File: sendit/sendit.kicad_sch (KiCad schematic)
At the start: 7 parts

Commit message: more work towards rev c board.
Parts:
- added H3, H4: MountingHole, MountingHole:MountingHole_2.7mm_M2.5_ISO14580, symbol Mechanical:MountingHole
- added R1, R2: 2.2k, Resistor_SMD:R_0603_1608Metric, symbol Device:R_Small_US
- H1, H2: footprint MountingHole:MountingHole_3.2mm_M3_ISO14580_Pad -> yarrboard:SMTSO30XXX; LCSC (none) -> C2916369; now in the parts list
- H5: renamed from H3; footprint MountingHole:MountingHole_3.2mm_M3_ISO14580_Pad -> yarrboard:SMTSO30XXX; LCSC (none) -> C2916369; now in the parts list
- H6: renamed from H4; footprint MountingHole:MountingHole_3.2mm_M3_ISO14580_Pad -> yarrboard:SMTSO30XXX; LCSC (none) -> C2916369; now in the parts list
- TP1, TP2: footprint TestPoint:TestPoint_THTPad_D2.0mm_Drill1.0mm -> TestPoint:TestPoint_THTPad_D1.5mm_Drill0.7mm
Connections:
- net +3.3V: now also R1.2, R2.2
- net SCL: now also R2.1
- net SDA: now also R1.1
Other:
- moved on the sheet: TP1, TP2

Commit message: power system work and layout
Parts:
- added H5: MountingHole, MountingHole:MountingHole_2.7mm_M2.5_ISO14580, symbol Mechanical:MountingHole
- added J1: Conn_01x04_MountingPin, yarrboard:JST_SH_BM04B-SRSS-TB_1x04-1MP_P1.00mm_Vertical, symbol Connector_Generic_MountingPin:Conn_01x04_MountingPin
- renumbered H5 to H6, H6 to H7
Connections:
- net +3.3V: now also J1.2 (Pin_2)
- net GND: now also J1.1 (Pin_1), J1.MP (MountPin)
- net SCL: now also J1.4 (Pin_4)
- net SDA: now also J1.3 (Pin_3)
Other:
- note added: "I2C / QWIIC"

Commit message: big change removing the usb hub and serial chip.
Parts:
- removed H4: MountingHole, MountingHole:MountingHole_2.7mm_M2.5_ISO14580, symbol Mechanical:MountingHole
- added J2: Conn_02x09_Odd_Even, Connector_PinHeader_2.54mm:PinHeader_2x09_P2.54mm_Vertical, symbol Connector_Generic:Conn_02x09_Odd_Even
- renumbered H5 to H4, H6 to H5, H7 to H6
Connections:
- net +3.3V: now also J2.2 (Pin_2)
- net GND: now also J2.1 (Pin_1)
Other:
- moved on the sheet: H4

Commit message: big routing push
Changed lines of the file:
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@@
 	(wire
 		(pts
-			(xy 153.67 87.63) (xy 157.48 87.63)
+			(xy 153.67 90.17) (xy 157.48 90.17)
 		)
 		(stroke
@@
 	(wire
 		(pts
-			(xy 146.05 77.47) (xy 157.48 77.47)
+			(xy 151.13 118.11) (xy 162.56 118.11)
 		)
 		(stroke
@@
 	(wire
 		(pts
-			(xy 153.67 90.17) (xy 157.48 90.17)
+			(xy 153.67 77.47) (xy 157.48 77.47)
 		)
 		(stroke
@@
 	(global_label "ADC_ALERT{slash}RDY2"
 		(shape input)
-		(at 153.67 90.17 180)
+		(at 153.67 77.47 180)
 		(fields_autoplaced yes)
 		(effects
@@
 		)
 		(property "Intersheetrefs" "${INTERSHEET_REFS}"
-			(at 134.4167 90.17 0)
+			(at 134.4167 77.47 0)
 			(effects
 				(font
@@
 	(global_label "ADC_ALERT{slash}RDY1"
 		(shape input)
-		(at 153.67 87.63 180)
+		(at 153.67 90.17 180)
 		(fields_autoplaced yes)
 		(effects
@@
 		)
 		(property "Intersheetrefs" "${INTERSHEET_REFS}"
-			(at 134.4167 87.63 0)
+			(at 134.4167 90.17 0)
 			(effects
 				(font
@@
 	)
 	(sheet
-		(at 133.35 74.93)
+		(at 138.43 115.57)
 		(size 12.7 3.81)
 		(exclude_from_sim no)
@@
 		)
 		(property "Sheetname" "Piezo"
-			(at 133.35 74.2184 0)
+			(at 138.43 114.8584 0)
 			(effects
 				(font
@@
 		)
 		(property "Sheetfile" "piezo.kicad_sch"
-			(at 133.35 79.3246 0)
+			(at 138.43 119.9646 0)
 			(effects
 				(font
@@
 		)
 		(pin "PIEZO" input
-			(at 146.05 77.47 0)
+			(at 151.13 118.11 0)
 			(effects
 				(font

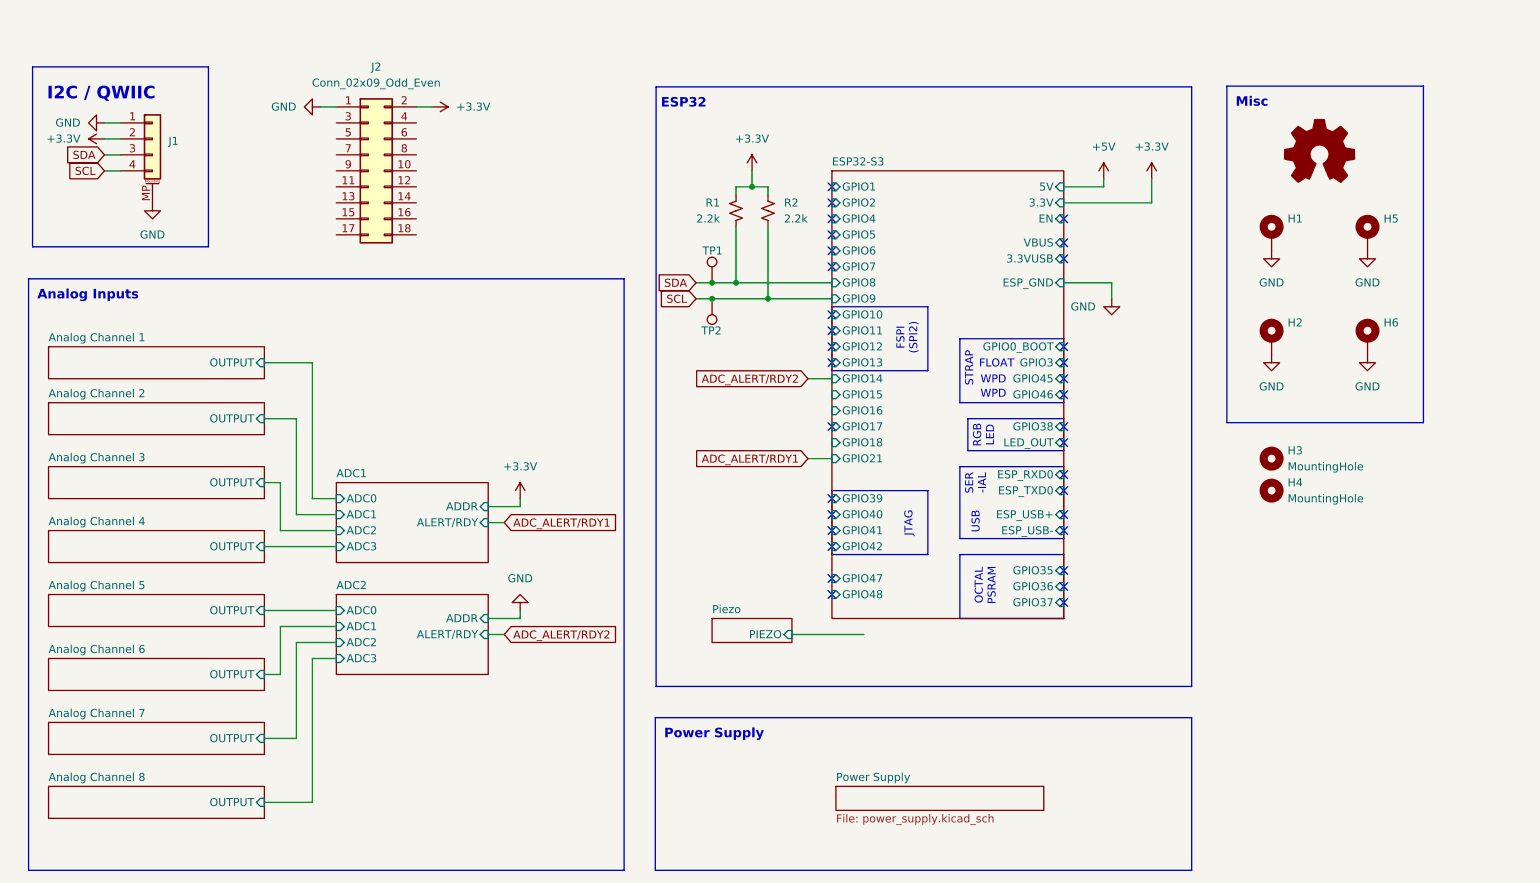
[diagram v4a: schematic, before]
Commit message: finished extra pin selection + routing
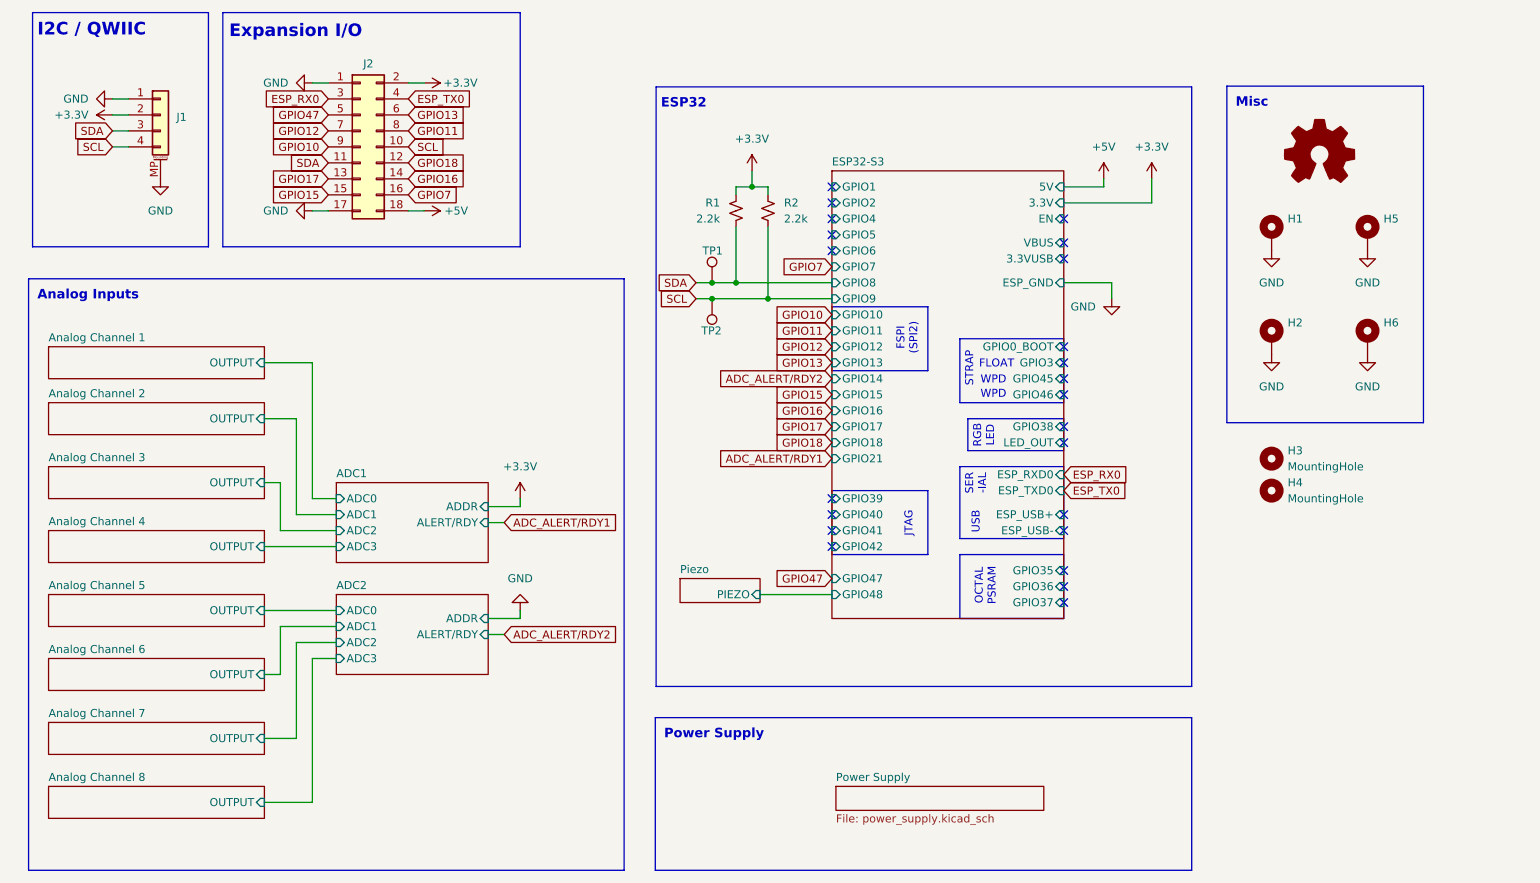
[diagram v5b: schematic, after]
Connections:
- net +5V: now also J2.18 (Pin_18)
- net GND: now also J2.17 (Pin_17)
- net SCL: now also J2.10 (Pin_10)
- net SDA: now also J2.11 (Pin_11)
- net GPIO18: now reaches J2.12 (Pin_12)
- net GPIO17: now reaches J2.13 (Pin_13)
- net GPIO16: now reaches J2.14 (Pin_14)
- net GPIO15: now reaches J2.15 (Pin_15)
- net GPIO7: now reaches J2.16 (Pin_16)
- net ESP_RX0: now reaches J2.3 (Pin_3)
- net ESP_TX0: now reaches J2.4 (Pin_4)
- net GPIO47: now reaches J2.5 (Pin_5)
- net GPIO13: now reaches J2.6 (Pin_6)
- net GPIO12: now reaches J2.7 (Pin_7)
- net GPIO11: now reaches J2.8 (Pin_8)
- net GPIO10: now reaches J2.9 (Pin_9)
- no-connect marks 33 -> 23
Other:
- note added: "Expansion I/O"
- moved on the sheet: J1, J2

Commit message: fixed erc errors
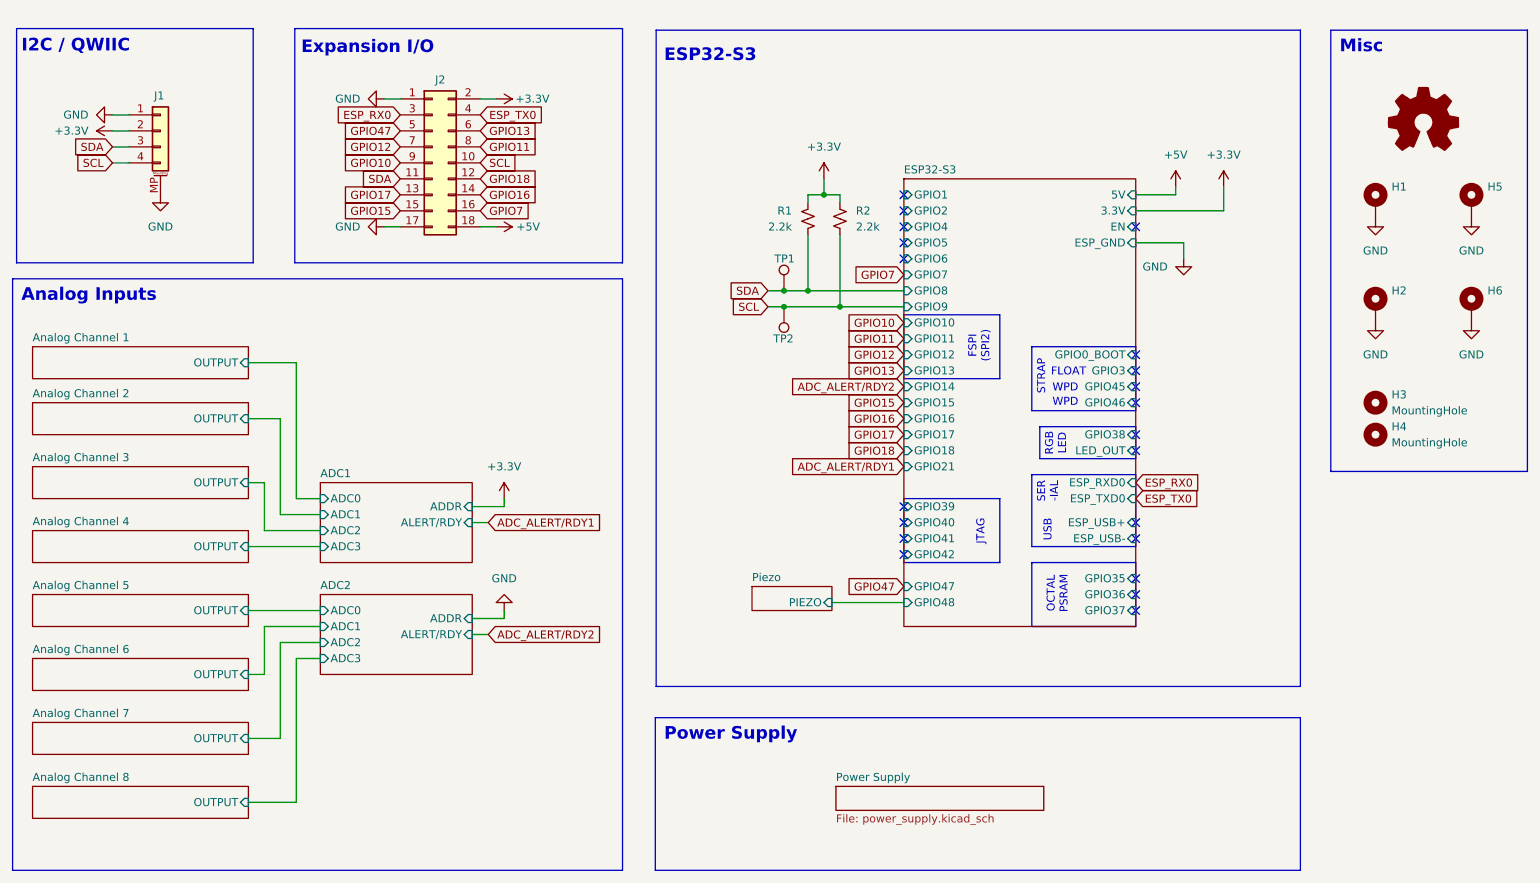
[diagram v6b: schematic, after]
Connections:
- no-connect marks 23 -> 21
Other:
- sheet ESP32-S3 ports: added none; removed 3.3VUSB, VBUS
- note added: "ESP32-S3"
- note removed: "ESP32"
- moved on the sheet: H1, H2, H3, H4, H5, H6, J1, J2, R1, R2, TP1, TP2

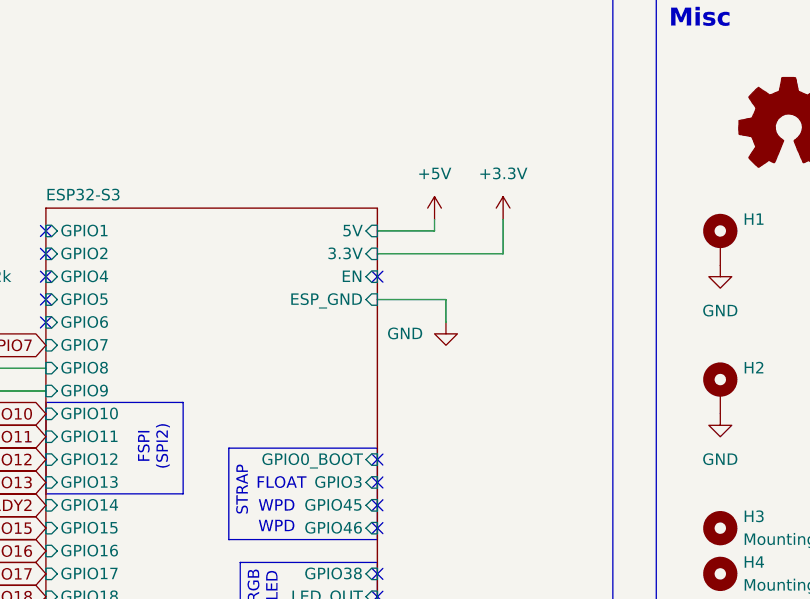
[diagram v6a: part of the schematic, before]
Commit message: double checked power supplies + gave esp32-s3 proper voltage/ground symbols
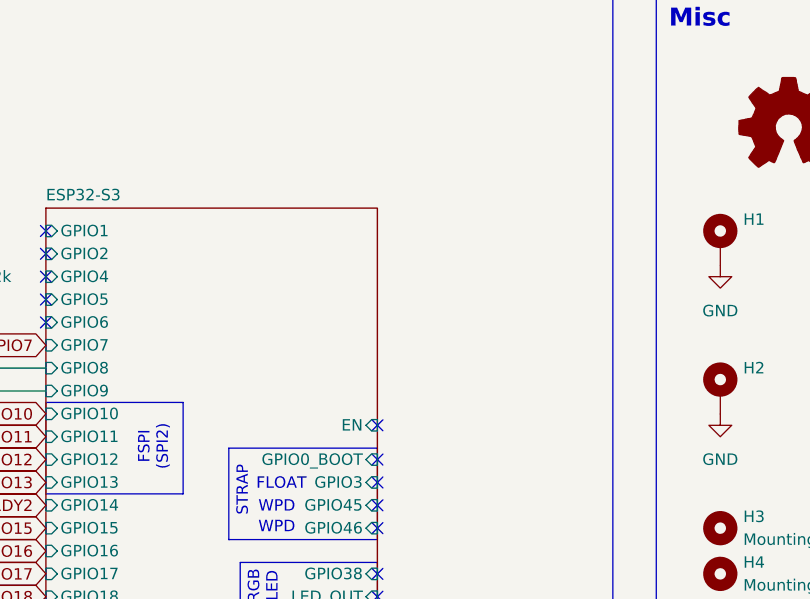
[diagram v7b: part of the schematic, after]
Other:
- sheet ESP32-S3 ports: added none; removed 3.3V, 5V, ESP_GND
